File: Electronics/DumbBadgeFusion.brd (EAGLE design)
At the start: 163.5 x 113 mm, 150 parts, among them IC1 74245MTC, IC2 74245MTC, IC3 74245MTC, SW1 SPST_TACT-KMR2, T1 MMUN2133LT1G, U1 ATSAMD21J18A-AUT, U2 TPS61090RSAR, U3 MCP73871, U4 FAN5333BSX, U5 TPD3E001SOT5, U6 MAX3232, X4 NX3215SA-32.768K-STD-MUA-8

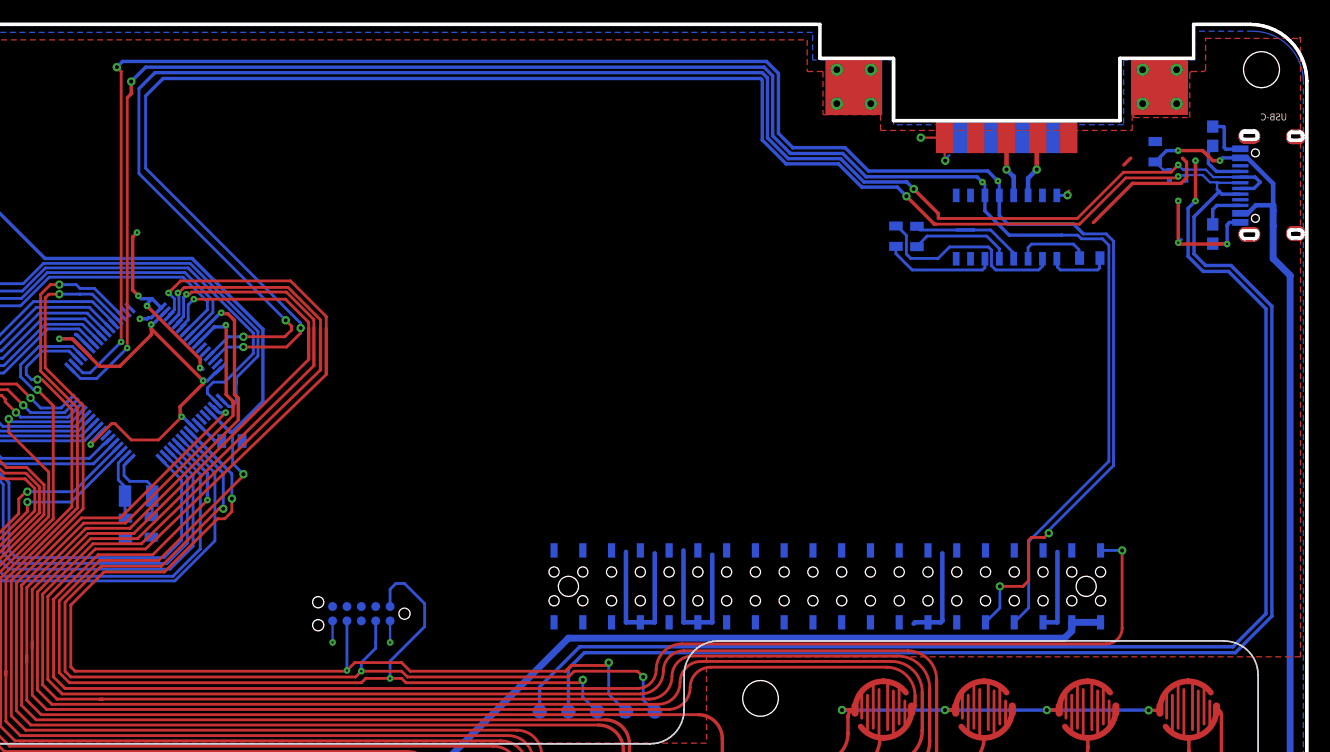
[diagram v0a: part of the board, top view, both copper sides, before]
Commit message: fixed Max3232
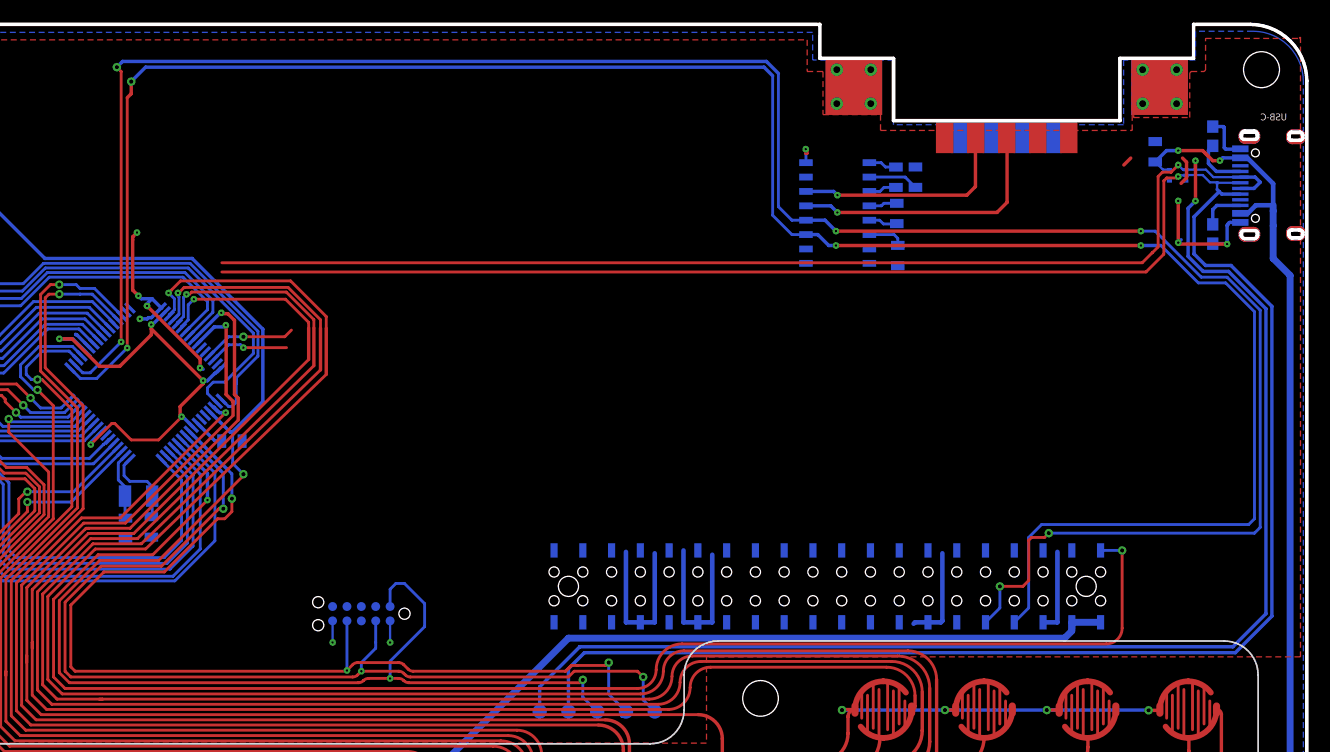
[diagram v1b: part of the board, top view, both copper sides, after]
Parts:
- added C13: 1.0uF, SparkFun-Capacitors:0805
- moved C22 18.5 mm to (127.2, 99.5), turned to 270 degrees
- moved U6 15.0 mm to (122.1, 96.3), turned to 270 degrees
- moved C24 5.49 mm to (128.9, 99.5), turned to 90 degrees
- moved C23 2.70 mm to (127.3, 96.3)
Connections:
- removed net N$52: U$5.P2, U6.14
- removed net N$61: C24.2, U6.6
- new net N$21: C13.1, U6.6
- new net N$22: U$5.P4, U6.14
- net GND: now also C13.2, C24.2, U$5.G1, U$5.G10, U$5.G11, U$5.G12, U$5.G2, U$5.G3, U$5.G4, U$5.G5, U$5.G6, U$5.G7, U$5.G8, U$5.G9; no longer U$5.P5
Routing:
- net USB_P: track 259.0 -> 220.7 mm, vias 4 -> 2
- net USB_N: track 262.2 -> 224.0 mm, vias 6 -> 4
- net UART_TX: track 164.8 -> 193.1 mm, vias 3 -> 4
- net UART_RX: track 169.8 -> 197.3 mm, vias 5 -> 6
- net N$22: track 0.00 -> 20.0 mm, vias 0 -> 1
- net N$23: track 5.50 -> 24.2 mm
- net N$1: track 17.9 -> 4.45 mm
- net N$61: track 9.97 -> 0.00 mm
- net N$12: track 11.6 -> 2.51 mm
- net 3V3: track 218.9 -> 210.5 mm
- net N$15: track 9.04 -> 2.57 mm
- net N$52: track 5.59 -> 0.00 mm, vias 1 -> 0
- net GND: track 191.5 -> 186.3 mm, vias 42 -> 40
- net N$6: track 6.57 -> 2.49 mm
- net N$21: track 0.00 -> 3.27 mm
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
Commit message: nother update
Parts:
- renumbered U$5 to DE9FEMALE
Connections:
- net N$22 renamed TXD
- net N$23 renamed RXD
- new net N$22: DE9FEMALE.P2, DE9FEMALE.P5, DE9FEMALE.P9
- net GND: now also DE9FEMALE.P1
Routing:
- net UART_RX: track 197.3 -> 167.8 mm
- net UART_TX: track 193.1 -> 163.8 mm
- net N$22: track 0.00 -> 16.6 mm, vias 0 -> 2
- net GND: track 186.3 -> 183.2 mm, vias 40 -> 39

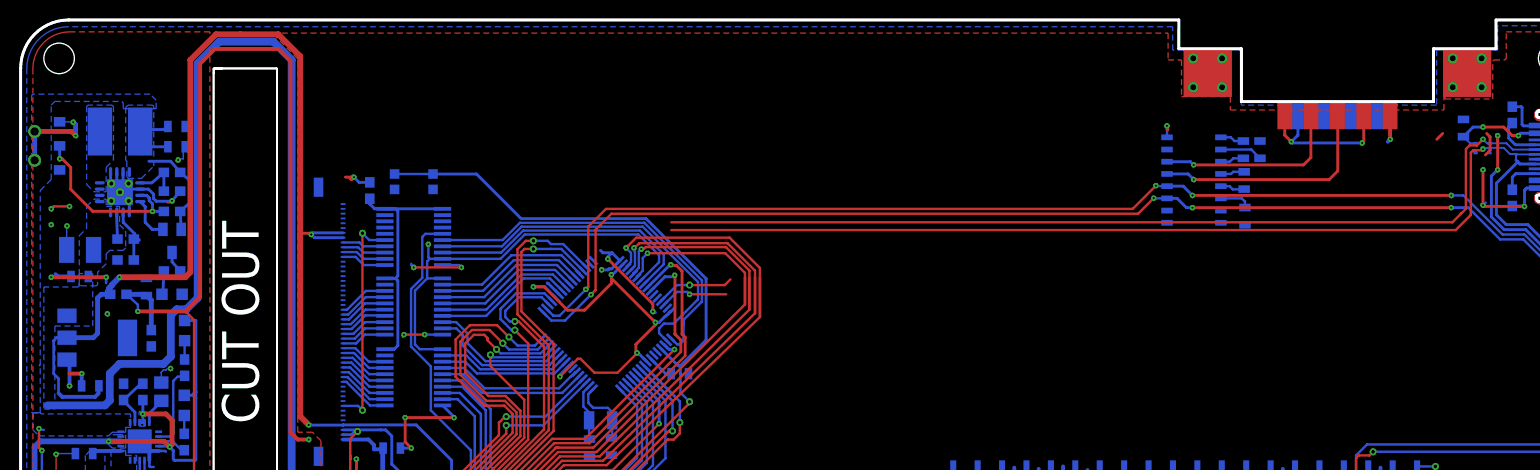
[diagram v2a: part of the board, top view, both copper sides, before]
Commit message: added bigger switch
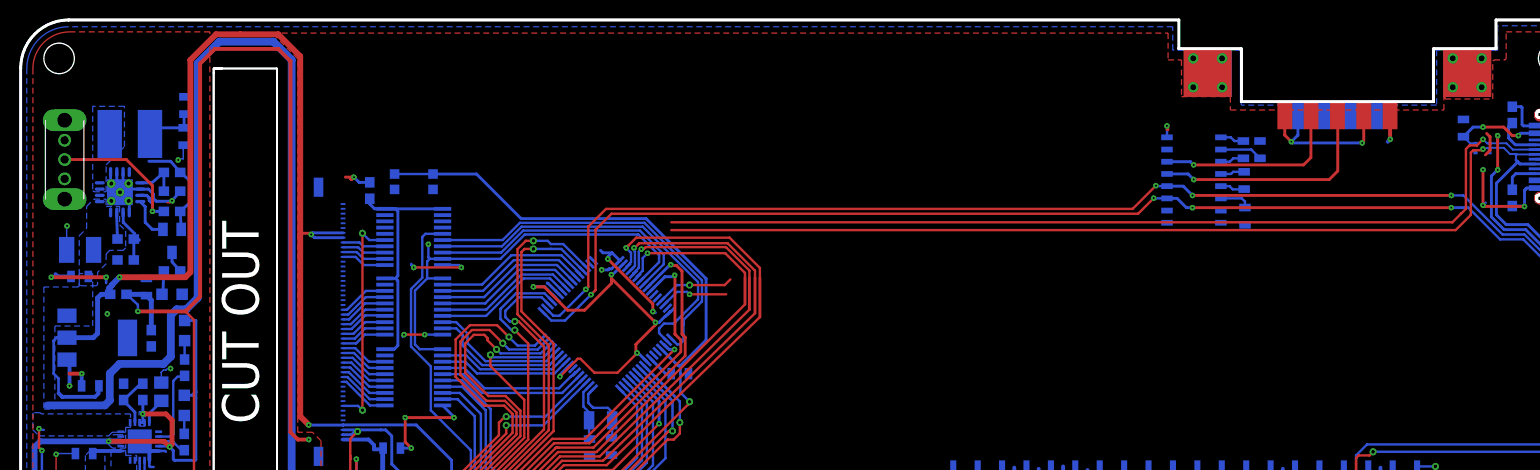
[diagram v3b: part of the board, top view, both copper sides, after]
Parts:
- removed S1: AYZ0102AGRLC, SamacSys_Parts:AYZ0102AGRLC
- added U$5: OS102011MA1QN1, FPC:OS102011MA1QN1
- moved C4 2.35 mm to (17.1, 104.1), turned to 90 degrees
- moved C2 1.33 mm to (17.0, 100.9), turned to 270 degrees
- moved L1 1.05 mm to (11.4, 101.1)
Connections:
- net ENABLE: now also U$5.P$2; no longer S1.2
- net GND: now also U$5.P$1; no longer S1.3, S1.4, S1.5
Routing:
- net GND: track 183.2 -> 205.0 mm, vias 39 -> 34
- net ENABLE: track 19.2 -> 17.5 mm, vias 2 -> 1
- net 3V3: track 210.5 -> 209.6 mm
- net VBAT: track 52.3 -> 51.7 mm

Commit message: starting rerouting
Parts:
- moved IC1 14.3 mm to (55.2, 83.2)
- moved IC2 14.3 mm to (55.2, 75.8)
- moved IC3 14.3 mm to (55.2, 90.4)
- moved SW1 14.3 mm to (55.2, 96.2)
- moved R19 14.3 mm to (50.6, 95.2)
- moved C27 13.7 mm to (72.8, 69.5)
- moved X4 13.7 mm to (74.0, 72.2)
- moved C26 13.7 mm to (75.1, 69.5)
- moved C12 13.0 mm to (81.6, 76.2)
- moved FPC50CONN 13.0 mm to (46.3, 81.6)
- moved U1 13.0 mm to (74.0, 81.3)
- moved C10 11.0 mm to (47.3, 61.8), turned to 270 degrees
- moved D1 7.00 mm to (45.0, 61.7), turned to 270 degrees
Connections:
- net DB00: now also FPC50CONN.A36, IC1.18; no longer FPC50CONN.A13, IC2.11
- net DB01: now also FPC50CONN.A35, IC1.17; no longer FPC50CONN.A14, IC2.12
- net DB02: now also FPC50CONN.A34, IC1.16; no longer FPC50CONN.A15, IC2.13
- net DB03: now also FPC50CONN.A33, IC1.15; no longer FPC50CONN.A16, IC2.14
- net DB04: now also FPC50CONN.A32, IC1.14; no longer FPC50CONN.A17, IC2.15
- net DB05: now also FPC50CONN.A31, IC1.13; no longer FPC50CONN.A18, IC2.16
- net DB06: now also FPC50CONN.A30, IC1.12; no longer FPC50CONN.A19, IC2.17
- net DB07: now also FPC50CONN.A29, IC1.11; no longer FPC50CONN.A20, IC2.18
- net DB08: now also FPC50CONN.A28, IC2.18; no longer FPC50CONN.A21, IC1.11
- net DB09: now also FPC50CONN.A27, IC2.17; no longer FPC50CONN.A22, IC1.12
- net DB10: now also FPC50CONN.A26, IC2.16; no longer FPC50CONN.A23, IC1.13
- net DB11: now also FPC50CONN.A25, IC2.15; no longer FPC50CONN.A24, IC1.14
- net DB12: now also FPC50CONN.A24, IC2.14; no longer FPC50CONN.A25, IC1.15
- net DB13: now also FPC50CONN.A23, IC2.13; no longer FPC50CONN.A26, IC1.16
- net DB14: now also FPC50CONN.A22, IC2.12; no longer FPC50CONN.A27, IC1.17
- net DB15: now also FPC50CONN.A21, IC2.11; no longer FPC50CONN.A28, IC1.18
- net GND: now also FPC50CONN.A13, FPC50CONN.A14, FPC50CONN.A15, FPC50CONN.A16, FPC50CONN.A17, FPC50CONN.A18, FPC50CONN.A19, FPC50CONN.A20; no longer FPC50CONN.A29, FPC50CONN.A30, FPC50CONN.A31, FPC50CONN.A32, FPC50CONN.A33, FPC50CONN.A34, FPC50CONN.A35, FPC50CONN.A36
- net LCD0: now also IC1.2; no longer IC2.9
- net LCD1: now also IC1.3; no longer IC2.8
- net LCD10: now also IC2.4; no longer IC1.7
- net LCD11: now also IC2.5; no longer IC1.6
- net LCD12: now also IC2.6; no longer IC1.5
- net LCD13: now also IC2.7; no longer IC1.4
- net LCD14: now also IC2.8; no longer IC1.3
- net LCD15: now also IC2.9; no longer IC1.2
- net LCD2: now also IC1.4; no longer IC2.7
- net LCD3: now also IC1.5; no longer IC2.6
- net LCD4: now also IC1.6; no longer IC2.5
- net LCD5: now also IC1.7; no longer IC2.4
- net LCD6: now also IC1.8; no longer IC2.3
- net LCD7: now also IC1.9; no longer IC2.2
- net LCD8: now also IC2.2; no longer IC1.9
- net LCD9: now also IC2.3; no longer IC1.8
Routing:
- net USB_P: track 220.7 -> 139.1 mm
- net USB_N: track 224.0 -> 142.7 mm
- net RESET: track 145.5 -> 66.4 mm, vias 3 -> 2
- net KEYCOLUM0: track 439.6 -> 376.5 mm, vias 9 -> 8
- net LCD_RESET: track 62.9 -> 0.00 mm
- net KEYCOLUM1: track 404.3 -> 342.6 mm, vias 7 -> 6
- net KEYCOLUM2: track 353.9 -> 293.3 mm, vias 6 -> 5
- net KEYCOLUM3: track 333.6 -> 273.7 mm, vias 3 -> 2
- net UART_RX: track 167.8 -> 110.4 mm
- net UART_TX: track 163.8 -> 106.7 mm
- net KEYROW8: track 250.8 -> 202.4 mm, vias 12 -> 11
- net LEDK: track 53.6 -> 5.69 mm, vias 2 -> 0
- net KEYROW5: track 168.7 -> 120.8 mm, vias 10 -> 9
- net KEYCOLUM5: track 356.8 -> 309.6 mm, vias 5 -> 4
- net KEYROW4: track 356.5 -> 309.8 mm, vias 13 -> 12
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
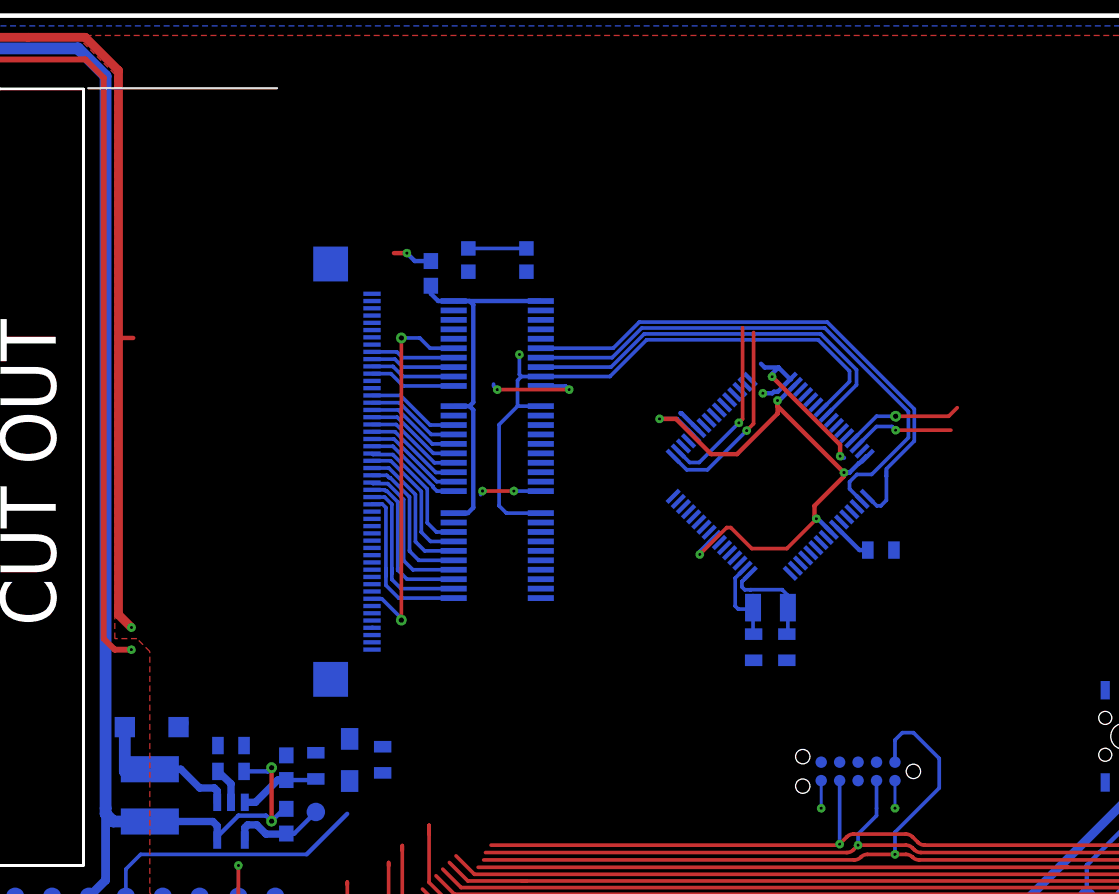
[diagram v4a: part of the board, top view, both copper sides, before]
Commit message: fixed FPC distance
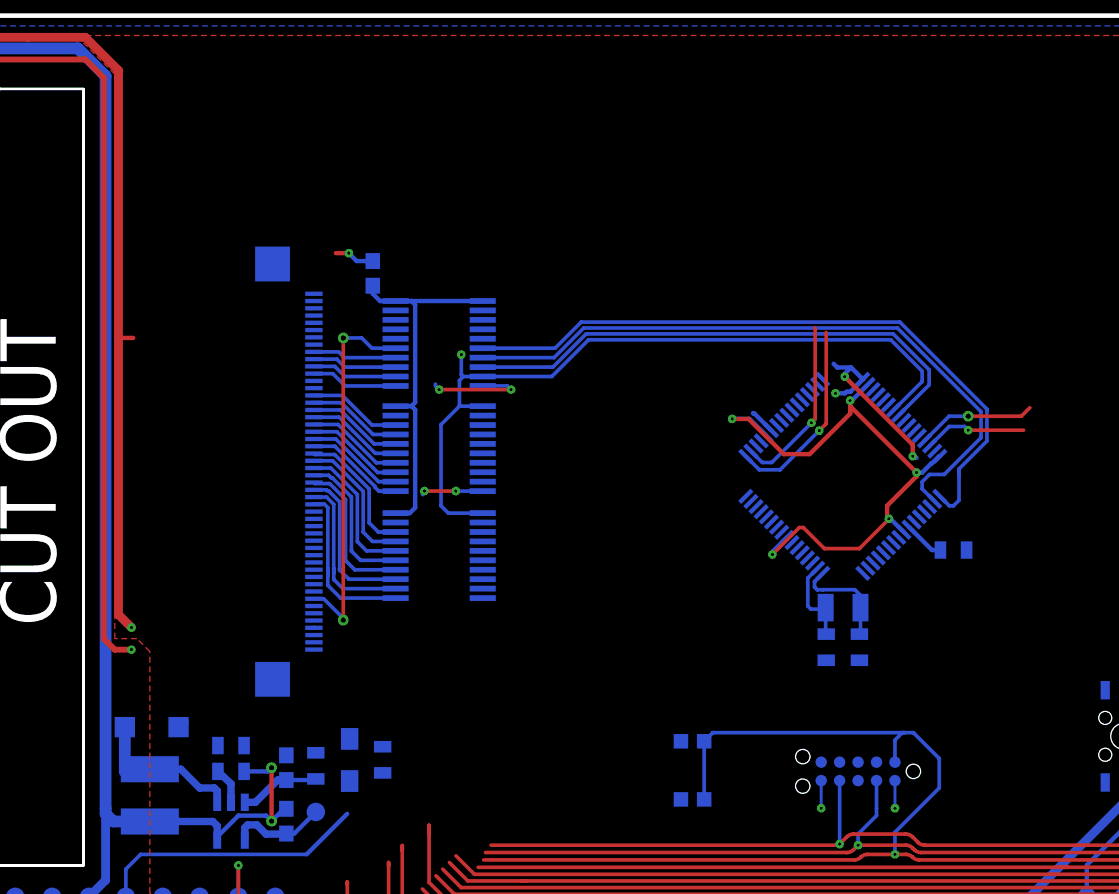
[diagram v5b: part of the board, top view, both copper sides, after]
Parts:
- moved SW1 37.6 mm to (68.6, 61.0), turned to 90 degrees
- moved C12 5.00 mm to (86.6, 76.2)
- moved C26 5.00 mm to (80.1, 69.5)
- moved C27 5.00 mm to (77.8, 69.5)
- moved U1 5.00 mm to (79.0, 81.3)
- moved X4 5.00 mm to (79.0, 72.2)
- moved FPC50CONN 4.00 mm to (42.3, 81.6)
- moved IC1 4.00 mm to (51.2, 83.2)
- moved IC2 4.00 mm to (51.2, 75.8)
- moved IC3 4.00 mm to (51.2, 90.4)
- moved R19 4.00 mm to (46.6, 95.2)
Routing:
- net RESET: track 66.4 -> 80.4 mm
- net LCD_W/R: track 27.7 -> 36.7 mm
- net LCD_D/C: track 37.4 -> 46.4 mm
- net LCD_CS: track 38.1 -> 47.1 mm
- net LCD_RD: track 43.8 -> 52.8 mm

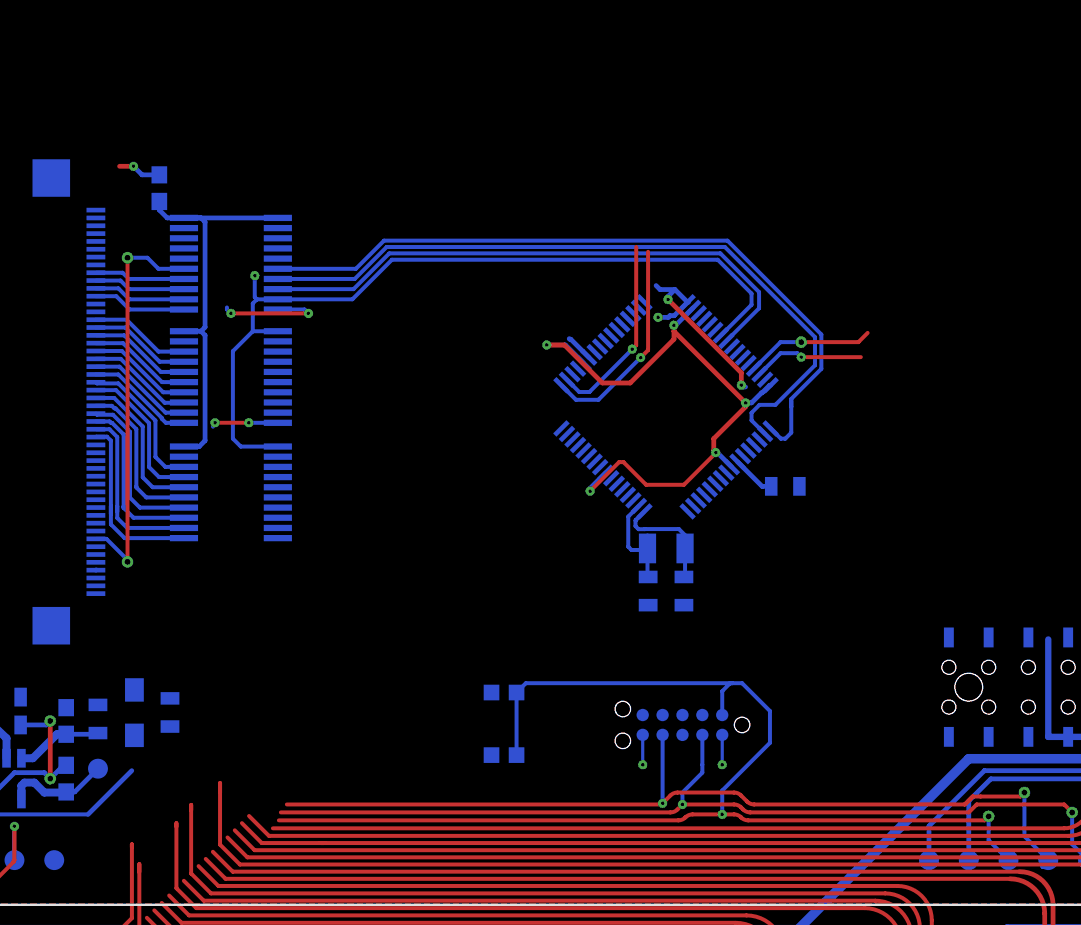
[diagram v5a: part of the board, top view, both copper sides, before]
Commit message: routed LCD bus
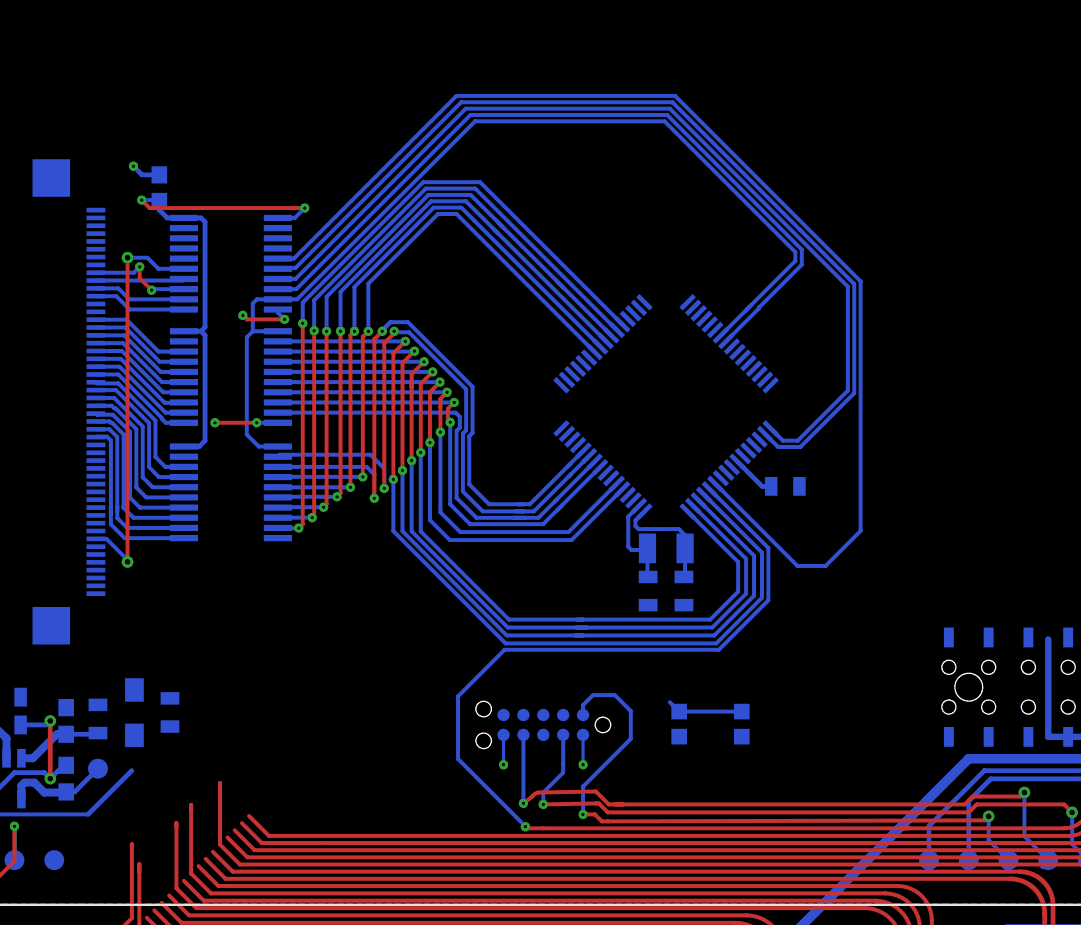
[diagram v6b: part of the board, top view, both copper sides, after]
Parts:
- moved SW1 13.2 mm to (81.8, 61.0), turned to 0 degrees
- moved TAG-CONNECT 8.89 mm to (71.1, 61.0)
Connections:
- net CS: now also IC3.13; no longer IC3.14
- net D/C: now also IC3.14; no longer IC3.13
- net LCD_CS: now also IC3.7; no longer IC3.6
- net LCD_D/C: now also IC3.6; no longer IC3.7
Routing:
- net LCD_RESET: track 0.00 -> 74.8 mm
- net LCD0: track 0.00 -> 56.7 mm, vias 0 -> 2
- net LCD1: track 0.00 -> 54.9 mm, vias 0 -> 2
- net LCD2: track 0.00 -> 53.4 mm, vias 0 -> 2
- net LCD3: track 0.00 -> 50.6 mm, vias 0 -> 2
- net LCD9: track 0.00 -> 43.5 mm, vias 0 -> 2
- net LCD15: track 0.00 -> 43.3 mm, vias 0 -> 2
- net 3V3: track 176.2 -> 133.4 mm, vias 10 -> 5
- net LCD8: track 0.00 -> 42.3 mm, vias 0 -> 2
- net LCD14: track 0.00 -> 42.2 mm, vias 0 -> 2
- net LCD13: track 0.00 -> 42.1 mm, vias 0 -> 2
- net LCD12: track 0.00 -> 40.4 mm, vias 0 -> 2
- net LCD11: track 0.00 -> 39.0 mm, vias 0 -> 2
- net LCD10: track 0.00 -> 37.9 mm, vias 0 -> 2
- net RESET: track 80.4 -> 46.7 mm
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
